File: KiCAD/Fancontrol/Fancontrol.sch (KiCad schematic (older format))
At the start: 11 parts, among them J1 Conn_Power, J2 Conn_TempSensor, J3 Conn_Fan, J4 Conn_ICSP, Q1 TIP122, U1 ATtiny85-20SU

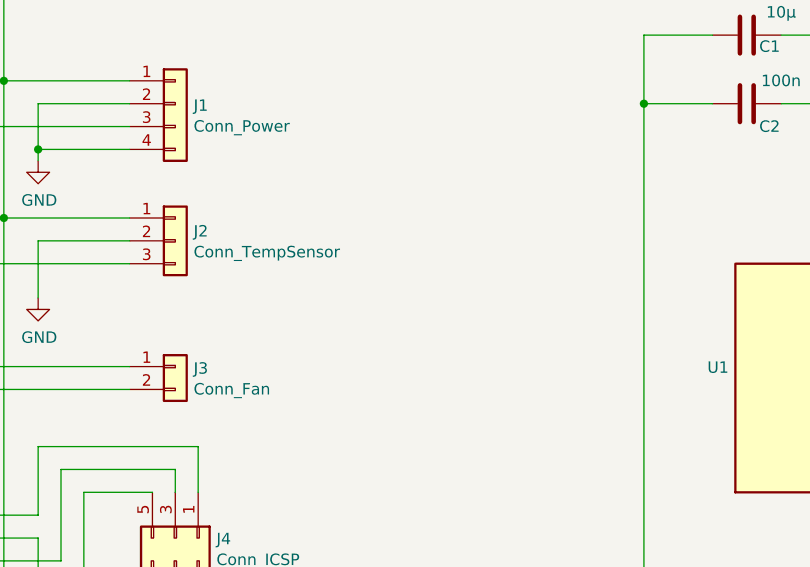
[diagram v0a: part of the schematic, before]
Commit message: Add text about sensor to schematic
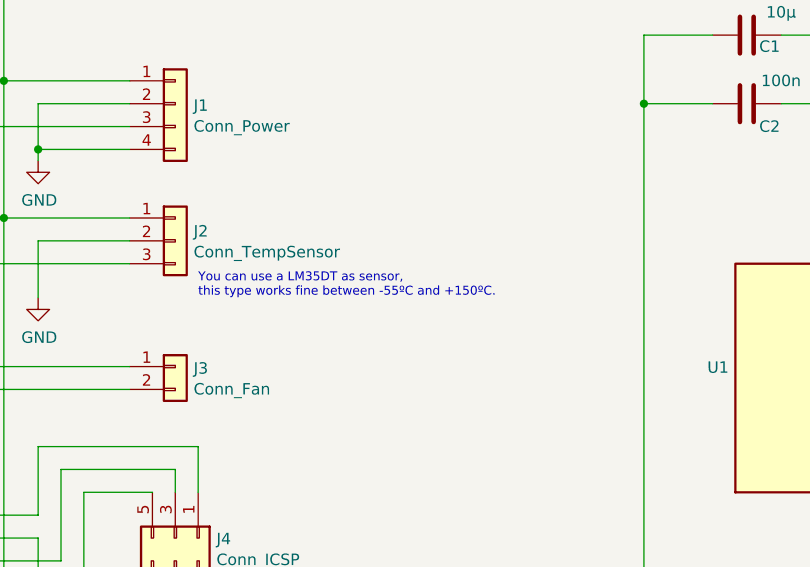
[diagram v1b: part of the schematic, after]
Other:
- note added: "You can use a LM35DT as sensor,\nthis type works fine between -55ºC and +150ºC."
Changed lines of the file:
@@
 Wire Wire Line
 	4600 7400 4600 6800
+Text Notes 3550 3450 0    39   ~ 0
+You can use a LM35DT as sensor,\nthis type works fine between -55ºC and +150ºC.
 $EndSCHEMATC

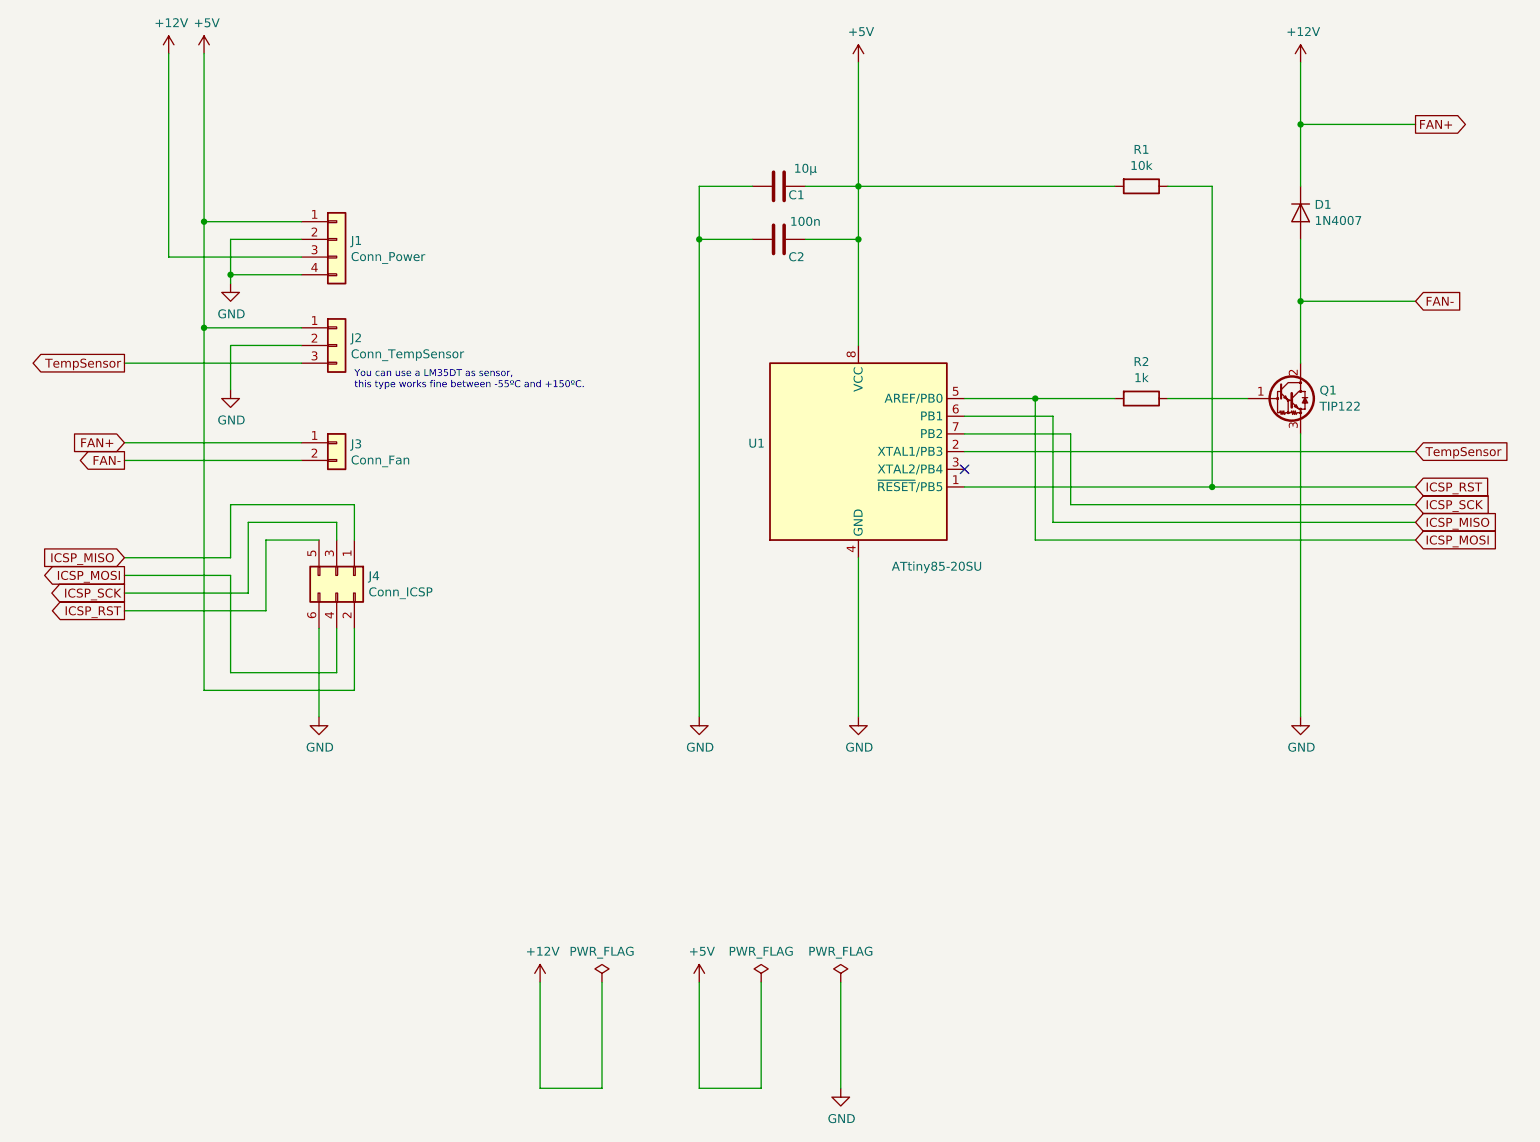
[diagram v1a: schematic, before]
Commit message: Update capacitor C1
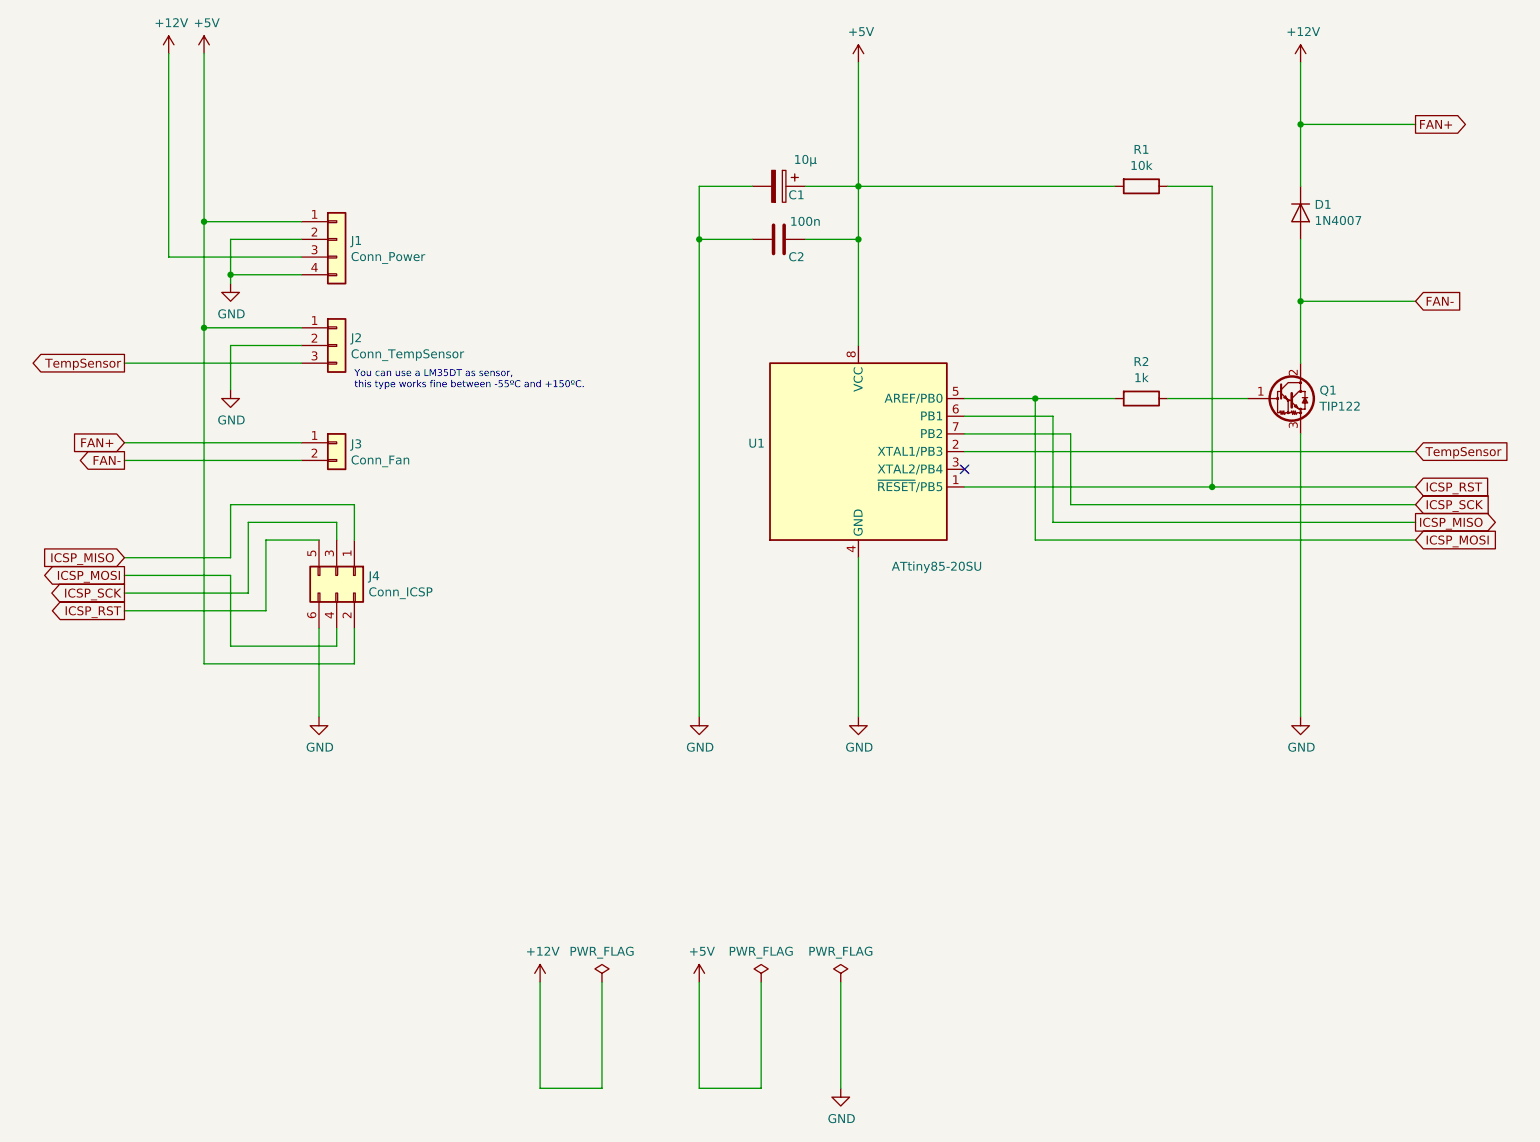
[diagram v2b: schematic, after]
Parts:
- removed C1: 10µ, Capacitors_SMD:C_0603_HandSoldering, symbol Device:C
- added C1: 10µ, Capacitors_SMD:C_0603_HandSoldering, symbol Device:CP
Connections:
- net +5V: now also C1.1
- net GND: now also C1.2
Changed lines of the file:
@@
-$EndComp
-$Comp
-L Device:C C1
-U 1 1 5E1FA283
-P 5950 2300
-F 0 "C1" V 6000 2400 50  0000 C CNN
-F 1 "10µ" V 5850 2450 50  0000 C CNN
-F 2 "Capacitors_SMD:C_0603_HandSoldering" H 5988 2150 50  0001 C CNN
-F 3 "~" H 5950 2300 50  0001 C CNN
-	1    5950 2300
-	0    1    1    0
 $EndComp
 $Comp
@@
 Text GLabel 9550 4100 2    50   Input ~ 0
 ICSP_SCK
-Text GLabel 9550 4200 2    50   Input ~ 0
+Text GLabel 9550 4200 2    50   Output ~ 0
 ICSP_MISO
 Text GLabel 9550 4300 2    50   Input ~ 0
@@
 	3050 4300 3050 4700
 Wire Wire Line
-	3450 4800 3450 5050
-Wire Wire Line
-	3450 5050 2850 5050
-Wire Wire Line
-	2850 5050 2850 4500
+	3450 4800 3450 4900
 $Comp
 L power:GND #PWR?
@@
 $EndComp
 Wire Wire Line
-	3550 4800 3550 5150
-Wire Wire Line
-	3550 5150 2700 5150
+	3550 4800 3550 5000
 Connection ~ 2700 3100
 Wire Wire Line
@@
 	2250 4500 2850 4500
 Wire Wire Line
-	2700 3100 2700 5150
+	2700 3100 2700 5000
 Wire Wire Line
 	2950 4600 2250 4600
@@
 Text Notes 3550 3450 0    39   ~ 0
 You can use a LM35DT as sensor,\nthis type works fine between -55ºC and +150ºC.
+Wire Wire Line
+	3450 4900 2850 4900
+Wire Wire Line
+	2850 4900 2850 4500
+Wire Wire Line
+	3550 5000 2700 5000
+$Comp
+L Device:CP C1
+U 1 1 5E31CA3E
+P 5950 2300
+F 0 "C1" V 6000 2400 50  0000 C CNN
+F 1 "10µ" V 5800 2450 50  0000 C CNN
+F 2 "Capacitors_SMD:C_0603_HandSoldering" H 5988 2150 50  0001 C CNN
+F 3 "~" H 5950 2300 50  0001 C CNN
+	1    5950 2300
+	0    1    1    0
+$EndComp
 $EndSCHEMATC
